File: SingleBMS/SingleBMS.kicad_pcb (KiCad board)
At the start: 2 copper layers, 139.7 x 137.9 mm, 192 parts, among them J1 Conn_02x09_Top_Bottom, J2 Conn_02x09_Top_Bottom, J3 Conn_01x19, J4 Conn_01x19, J5 Conn_01x02, J6 Conn_01x08, J7 Conn_02x09_Top_Bottom, J8 Conn_01x02, Q1 2N7002, Q10 2N7002, Q11 2N7002, Q12 2N7002, Q13 2N7002, Q14 2N7002, Q15 2N7002, Q16 2N7002, Q2 2N7002, Q3 2N7002, Q4 2N7002, Q5 2N7002, Q6 2N7002, Q7 2N7002, Q8 2N7002, Q9 2N7002, U1 CD74HC4067M, U10 MCP23017_SP, U11 INA194, U12 MCP6004, U13 MCP6004, U14 MCP6004, U15 MCP6004, U16 PC817, U17 PC817, U18 PC817, U19 PC817, U2 PCF8574, U20 PC817, U21 PC817, U22 PC817, U23 PC817, U24 PC817, U25 PC817, U26 PC817, U27 PC817, U28 PC817, U29 PC817, U3 PCA9306, U30 PC817, U31 PC817, U4 ADS1115IDGS, U5 MCP6001-OT, U6 CD74HC4067M, U7 ESP32-DEVKITC-32D, U8 LM7805_TO220, U9 INA194

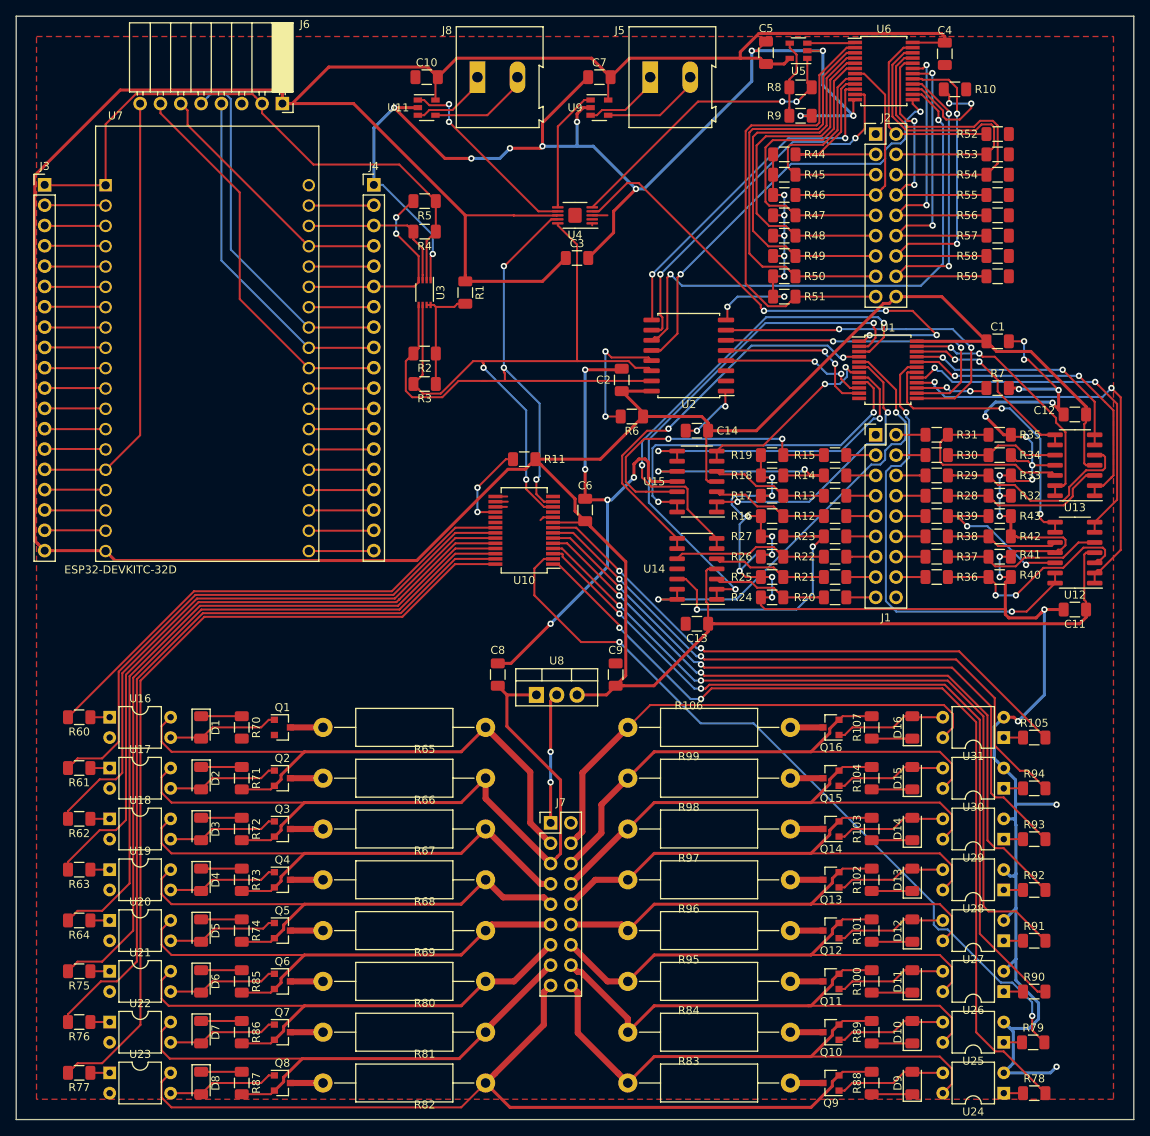
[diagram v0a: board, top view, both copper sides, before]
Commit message: Added parts for SMT, fixed voltage dividers, fixed footprint sizes
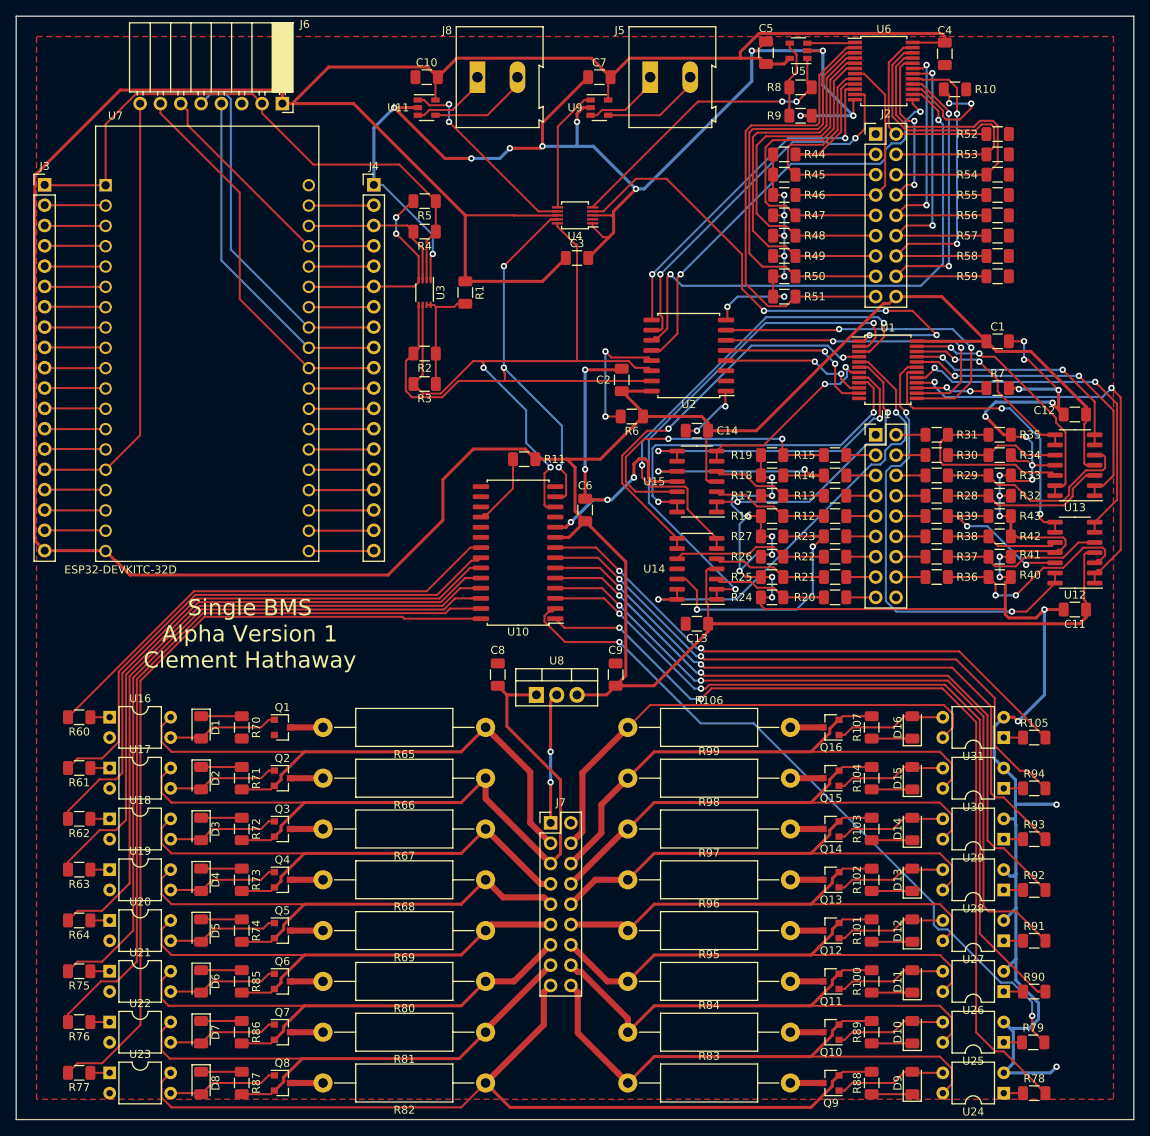
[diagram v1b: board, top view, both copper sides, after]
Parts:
- R100, R101, R102, R103, R104, R107, R70, R71, R72, R73, R74, R85, R86, R87, R88, R89: value 470R -> 270R
- R12: value 115k -> 300k
- R13: value 21.5k -> 240k
- R14: value 11k -> 100k
- R16: value 35.7k -> 100k
- R17: value 10k -> 120k
- R18: value 10k -> 100k
- R19: value 20k -> 300k
- R20: value 102K -> 91k
- R21: value 127K -> 180k
- R22: value 118K -> 110k
- R23: value 43.2k -> 120k
- R24: value 13.7K -> 13K
- R25: value 20K -> 30k
- R26: value 22.1k -> 22k
- R27: value 10.2k -> 30k
- R28: value 232k -> 330k
- R29, R37: value 174k -> 180k
- R30: value 133K -> 270k
- R31: value 84.5K -> 240k
- R32: value 20k -> 30k
- R33: value 16.5k -> 18k
- R34: value 14K -> 30k
- R35: value 10K -> 30k
- R36: value 158k -> 270k
- R38: value 137k -> 390k
- R39: value 205k -> 240k
- R40: value 10k -> 18k
- R41: value 11.8k -> 13k
- R42: value 10k -> 30k
- R43: value 16.2k -> 20k
- R8: value 40k -> 43k
- R9: value 10k -> 11k
- U10: footprint Package_SO:SSOP-28_5.3x10.2mm_P0.65mm -> Package_SO:SOIC-28W_7.5x17.9mm_P1.27mm
- U4: footprint Package_SO:MSOP-10-1EP_3x3mm_P0.5mm_EP1.68x1.88mm -> Package_SO:MSOP-10_3x3mm_P0.5mm
- moved U10 2.90 mm to (194.8, 79.0)
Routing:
- net GND: track 548.7 -> 526.9 mm
- net /passiveBalance16/Bal10: track 96.7 -> 90.3 mm
- net Vcc: track 562.4 -> 567.0 mm
- net /passiveBalance16/Bal8: track 105.0 -> 100.5 mm
- net /passiveBalance16/Bal7: track 98.7 -> 94.3 mm
- net /passiveBalance16/Bal6: track 93.6 -> 89.4 mm
- net /passiveBalance16/Bal5: track 87.9 -> 84.0 mm
- net /passiveBalance16/Bal4: track 81.5 -> 77.9 mm
- net /passiveBalance16/Bal3: track 75.8 -> 72.5 mm
- net /passiveBalance16/Bal2: track 70.7 -> 67.6 mm
- net /passiveBalance16/Bal9: track 112.9 -> 109.9 mm
- net /passiveBalance16/Bal1: track 63.2 -> 60.4 mm
- net /passiveBalance16/Bal11: track 100.5 -> 97.7 mm
- net Net-(U1-Pad1): track 62.6 -> 65.3 mm
- net /passiveBalance16/Bal12: track 95.8 -> 93.5 mm
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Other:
- board text added: "Single BMS Alpha Version 1 Clement Hathaway"
